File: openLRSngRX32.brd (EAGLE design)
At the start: 43 x 39.4 mm, 60 parts, among them IC1 STM32F10XCXT6, IC2 REG1117, U1 MPU-6000QFN-24, Y1 8MHz

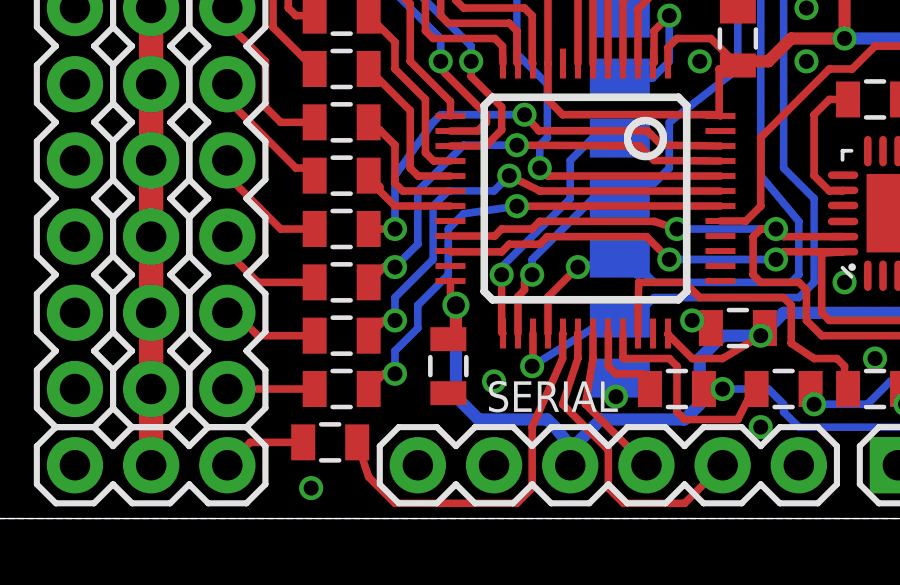
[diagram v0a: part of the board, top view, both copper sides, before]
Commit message: Fix missing BOOT1 pulldown.
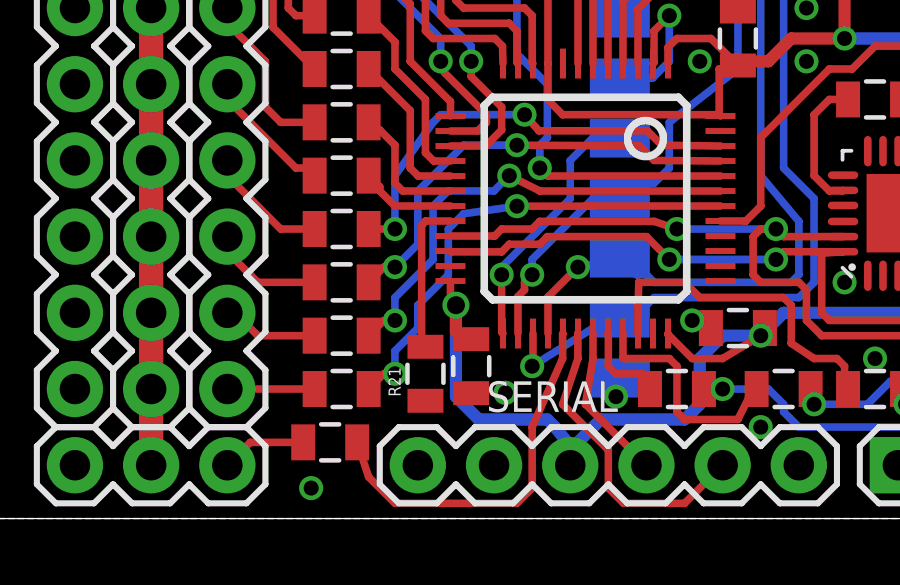
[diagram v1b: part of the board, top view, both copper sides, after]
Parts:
- added R21: 10k, SparkFun-Resistors:0805
- moved C7 0.76 mm to (15.7, 5.08)
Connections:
- new net BOOT1: IC1.20, R21.2
- net GND: now also R21.1
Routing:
- net BOOT1: track 0.00 -> 5.21 mm
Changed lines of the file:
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@@
 <attribute name="VALUE" x="18.034" y="19.431" size="0.4064" layer="27" rot="R180"/>
 </element>
-<element name="C7" library="SparkFun-Capacitors" package="0805" value="" x="14.986" y="5.08" smashed="yes" rot="R270">
-<attribute name="VALUE" x="13.589" y="6.096" size="0.4064" layer="27" rot="R270"/>
+<element name="C7" library="SparkFun-Capacitors" package="0805" value="" x="15.748" y="5.08" smashed="yes" rot="R270">
+<attribute name="VALUE" x="14.351" y="6.096" size="0.4064" layer="27" rot="R270"/>
 </element>
 <element name="R13" library="SparkFun-Resistors" package="0805" value="4k7" x="35.052" y="4.572" smashed="yes" rot="R90"/>
@@
 </element>
 <element name="R20" library="SparkFun-Resistors" package="0805" value="330R" x="22.606" y="4.318" smashed="yes" rot="R180"/>
+<element name="R21" library="SparkFun-Resistors" package="0805" value="10k" x="14.224" y="4.826" rot="R90"/>
 </elements>
 <signals>
@@
 <wire x1="33.782" y1="12.192" x2="34.152" y2="12.192" width="0.254" layer="1"/>
 <wire x1="34.152" y1="12.192" x2="34.29" y2="12.33" width="0.254" layer="1"/>
-<polygon width="0.254" layer="1" thermals="no">
+<polygon width="0.254" layer="1">
 <vertex x="0" y="0"/>
 <vertex x="42.926" y="0"/>
@@
 <vertex x="0" y="39.624"/>
 </polygon>
-<polygon width="0.254" layer="16" thermals="no">
+<polygon width="0.254" layer="16">
 <vertex x="0" y="0"/>
 <vertex x="42.926" y="0"/>
@@
 <contactref element="LED2" pad="C"/>
 <via x="23.114" y="6.604" extent="1-16" drill="0.5"/>
-<via x="16.51" y="4.572" extent="1-16" drill="0.5"/>
+<via x="16.891" y="4.191" extent="1-16" drill="0.5"/>
+<contactref element="R21" pad="1"/>
+<wire x1="15.058" y1="8.418" x2="15.748" y2="4.18" width="0" layer="19" extent="1-1"/>
 </signal>
 <signal name="VCC">
@@
 <via x="15.24" y="7.112" extent="1-16" drill="0.6"/>
 <wire x1="15.24" y1="7.112" x2="15.24" y2="6.234" width="0.4064" layer="1"/>
-<wire x1="15.24" y1="6.234" x2="14.986" y2="5.98" width="0.4064" layer="1"/>
+<wire x1="15.24" y1="6.234" x2="15.748" y2="5.98" width="0.4064" layer="1"/>
 <wire x1="15.058" y1="7.918" x2="15.058" y2="7.294" width="0.254" layer="1"/>
 <wire x1="15.058" y1="7.294" x2="15.24" y2="7.112" width="0.254" layer="1"/>
@@
 <wire x1="28.194" y1="4.434" x2="28.31" y2="4.318" width="0.254" layer="1"/>
 </signal>
+<signal name="BOOT1">
+<contactref element="IC1" pad="20"/>
+<contactref element="R21" pad="2"/>
+<wire x1="15.058" y1="9.918" x2="14.224" y2="9.918" width="0.254" layer="1"/>
+<wire x1="14.224" y1="9.918" x2="14.224" y2="9.906" width="0.254" layer="1"/>
+<wire x1="14.224" y1="9.906" x2="14.097" y2="9.779" width="0.254" layer="1"/>
+<wire x1="14.097" y1="9.779" x2="14.097" y2="5.726" width="0.254" layer="1"/>
+<wire x1="14.097" y1="5.726" x2="14.224" y2="5.726" width="0.254" layer="1"/>
+</signal>
 </signals>

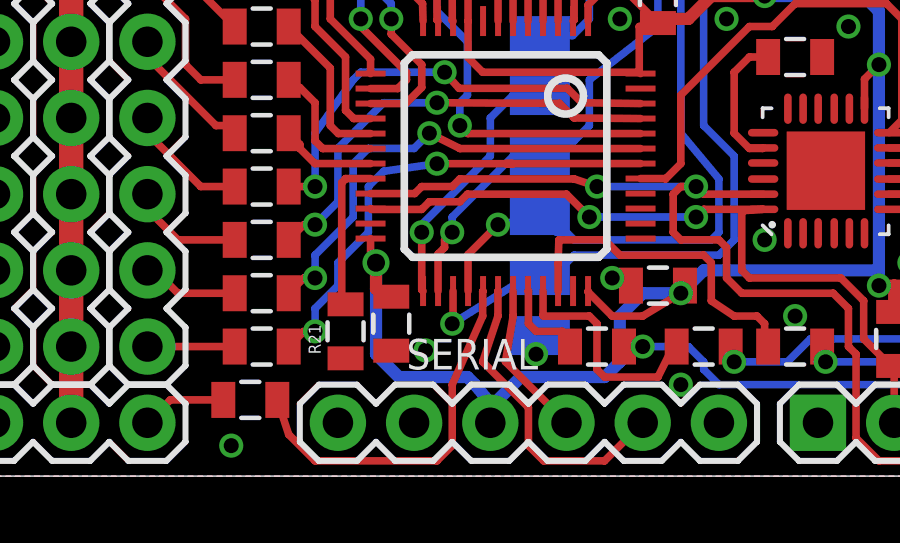
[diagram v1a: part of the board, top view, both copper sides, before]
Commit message: missed some airwires on last commit...
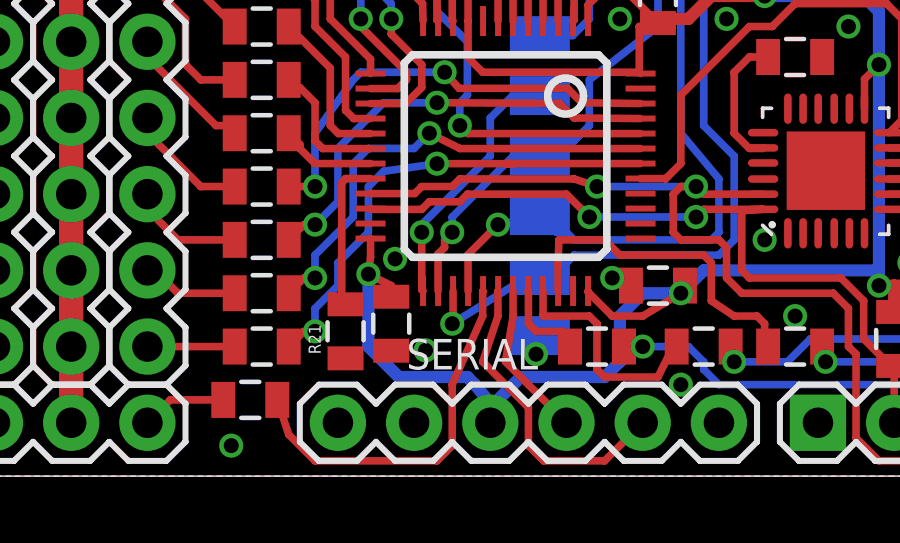
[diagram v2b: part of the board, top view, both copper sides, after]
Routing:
- net GND: track 5.12 -> 5.79 mm, vias 20 -> 21
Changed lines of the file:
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@@
 <via x="16.891" y="4.191" extent="1-16" drill="0.5"/>
 <contactref element="R21" pad="1"/>
-<wire x1="15.058" y1="8.418" x2="15.748" y2="4.18" width="0" layer="19" extent="1-1"/>
+<via x="15.875" y="7.239" extent="1-16" drill="0.5"/>
+<wire x1="20.574" y1="4.064" x2="20.574" y2="4.556" width="0.254" layer="16"/>
+<wire x1="20.574" y1="4.556" x2="20.702" y2="4.684" width="0.254" layer="16"/>
 </signal>
 <signal name="VCC">
@@
 <wire x1="18.542" y1="3.048" x2="18.288" y2="3.302" width="0.4064" layer="16"/>
 <wire x1="18.288" y1="3.302" x2="16.002" y2="3.302" width="0.4064" layer="16"/>
-<wire x1="16.002" y1="3.302" x2="15.24" y2="4.064" width="0.4064" layer="16"/>
-<wire x1="15.24" y1="4.064" x2="15.24" y2="7.112" width="0.4064" layer="16"/>
-<via x="15.24" y="7.112" extent="1-16" drill="0.6"/>
-<wire x1="15.24" y1="7.112" x2="15.24" y2="6.234" width="0.4064" layer="1"/>
-<wire x1="15.24" y1="6.234" x2="15.748" y2="5.98" width="0.4064" layer="1"/>
+<wire x1="16.002" y1="3.302" x2="14.986" y2="4.318" width="0.4064" layer="16"/>
+<wire x1="14.986" y1="4.318" x2="14.986" y2="6.731" width="0.4064" layer="16"/>
+<via x="14.986" y="6.731" extent="1-16" drill="0.5"/>
 <wire x1="15.058" y1="7.918" x2="15.058" y2="7.294" width="0.254" layer="1"/>
-<wire x1="15.058" y1="7.294" x2="15.24" y2="7.112" width="0.254" layer="1"/>
+<wire x1="15.058" y1="7.294" x2="14.986" y2="6.731" width="0.254" layer="1"/>
 <wire x1="5.08" y1="34.798" x2="5.08" y2="37.338" width="0.8128" layer="1"/>
 <wire x1="37.592" y1="1.778" x2="37.592" y2="4.826" width="0.4064" layer="1"/>
@@
 <wire x1="25.4" y1="6.096" x2="25.4" y2="6.212" width="0.254" layer="1"/>
 <wire x1="25.4" y1="6.212" x2="25.538" y2="6.35" width="0.254" layer="1"/>
+<wire x1="15.748" y1="5.98" x2="15.748" y2="6.35" width="0.254" layer="1"/>
+<wire x1="15.748" y1="6.35" x2="14.986" y2="6.731" width="0.254" layer="1"/>
 </signal>
 <signal name="N$1">
